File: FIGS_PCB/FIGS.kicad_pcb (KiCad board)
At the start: 2 copper layers, 54.1 x 52.8 mm, 66 parts, among them IC1 CY8C4245AXI-483, J1 CAPSENSE_CON, J10 HAPTIC_M, J2 FINGCONN, J3 BLUTH, J4 IMU, J5 SERVO_0, J6 SERVO_1, J7 SERVO_2, J8 PROGRAMMER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

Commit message: PCB changed
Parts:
- removed R1, R3, R5, R7: 5.6k, Resistor_SMD:R_1206_3216Metric_Pad1.30x1.75mm_HandSolder
- removed R10, R9: 0, Resistor_SMD:R_1206_3216Metric_Pad1.30x1.75mm_HandSolder
- removed R2, R4, R6, R8: nc, Resistor_SMD:R_1206_3216Metric_Pad1.30x1.75mm_HandSolder
- added H1: MountingHole, MountingHole:MountingHole_2.7mm, F.Cu at (33.0, 38.0)
- added H2: MountingHole, MountingHole:MountingHole_2.7mm, F.Cu at (35.0, 76.0)
- added H3: MountingHole, MountingHole:MountingHole_2.7mm, F.Cu at (80.0, 39.5)
- added TP1: TestPoint, TestPoint:TestPoint_Pad_D3.0mm, F.Cu at (64.5, 54.9)
- added TP2: TestPoint, TestPoint:TestPoint_Pad_D3.0mm, F.Cu at (40.6, 73.9)
- C11, C4: footprint Capacitor_Tantalum_SMD:CP_EIA-7260-28_AVX-M_Pad2.68x6.30mm_HandSolder -> Capacitor_Tantalum_SMD:CP_EIA-7132-20_AVX-U_Pad2.72x3.50mm_HandSolder
- C2, C3, C5, C6, R11, R14, R18, R20, R24, R26: moved to B.Cu
- J1: footprint Connector_PinHeader_1.27mm:PinHeader_1x08_P1.27mm_Horizontal -> Connector_PinHeader_2.54mm:PinHeader_1x08_P2.54mm_Horizontal
- J10: footprint Connector_PinHeader_1.27mm:PinHeader_1x02_P1.27mm_Horizontal -> Connector_PinHeader_2.54mm:PinHeader_1x02_P2.54mm_Horizontal; moved to F.Cu
- J2: footprint Connector_PinHeader_1.27mm:PinHeader_2x04_P1.27mm_Vertical -> Connector_PinHeader_2.54mm:PinHeader_2x04_P2.54mm_Horizontal
- J3: footprint Connector_PinHeader_1.27mm:PinHeader_1x04_P1.27mm_Horizontal -> Connector_PinHeader_2.54mm:PinHeader_1x04_P2.54mm_Horizontal
- J4: footprint Connector_PinHeader_1.27mm:PinHeader_1x04_P1.27mm_Horizontal -> Connector_PinHeader_2.54mm:PinHeader_1x04_P2.54mm_Horizontal; moved to F.Cu
- J5, J6, J7, J9: footprint Connector_PinHeader_1.27mm:PinHeader_1x03_P1.27mm_Horizontal -> Connector_PinHeader_2.54mm:PinHeader_1x03_P2.54mm_Horizontal
- J8: footprint Connector_PinHeader_1.27mm:PinHeader_2x05_P1.27mm_Horizontal -> Connector_PinHeader_2.54mm:PinHeader_2x05_P2.54mm_Vertical; moved to F.Cu
- R15: moved to F.Cu
- moved BT1 57.7 mm to (32.5, 87.1)
- moved C4 54.9 mm to (43.7, 84.8)
- moved SW1 53.2 mm to (36.8, 87.1), turned to 90 degrees
- moved C7 42.6 mm to (47.2, 83.1), turned to 90 degrees
- moved U1 38.3 mm to (52.1, 82.1), turned to 90 degrees
- moved D7 37.8 mm to (38.4, 68.3), turned to 90 degrees
- moved R15 37.1 mm to (62.2, 77.5)
- moved J10 36.1 mm to (41.1, 69.6), turned to 180 degrees
- moved J2 33.0 mm to (32.0, 32.5), turned to 90 degrees
- moved D2 32.9 mm to (36.3, 42.7)
- moved D4 30.7 mm to (41.1, 40.1), turned to 270 degrees
- moved D1 30.6 mm to (36.3, 48.0)
- moved Q5 30.0 mm to (45.2, 66.8), turned to 90 degrees
- moved R28 29.7 mm to (45.7, 70.4), turned to 180 degrees
- moved D3 27.7 mm to (41.1, 45.5)
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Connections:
- IC1 pad 24: /Rx_1 -> /BT_UART_TX
- IC1 pad 25: /Tx_1 -> /BT_UART_RX
- J3 pad 1: +3V3 -> /BT_UART_RX
- J3 pad 3: /BT_UART_RX -> GNDA
- J3 pad 4: GNDA -> +3V3
- J4 pad 2: /IMU_SCL -> /IMU_SDA
- J4 pad 3: /IMU_SDA -> /IMU_SCL
- J5 pad 1: +BATT -> /CTRLS0
- J5 pad 2: /CTRLS0 -> +BATT
- J6 pad 1: +BATT -> /CTRLS1
- J6 pad 2: /CTRLS1 -> +BATT
- J7 pad 1: +BATT -> /CTRLS2
- J7 pad 2: /CTRLS2 -> +BATT
- J8 pad 1: +3V3 -> GNDA
- J8 pad 10: /KP_TX -> /TUNER_SDA
- J8 pad 2: GNDA -> +3V3
- J8 pad 3: /SWD_IO -> /XRES
- J8 pad 4: /XRES -> /SWD_IO
- J8 pad 5: /SWD_CLK -> Net-(J8-Pad5)
- J8 pad 6: Net-(J8-Pad6) -> /SWD_CLK
- J8 pad 7: /TUNER_SCL -> /KP_TX
- J8 pad 8: /KP_RX -> /TUNER_SCL
- J8 pad 9: /TUNER_SDA -> /KP_RX
- J9 pad 1: +BATT -> /CTRLS3
- J9 pad 2: /CTRLS3 -> +BATT
- R11 pad 2: /IMU_SDA -> /IMU_SCL
- R12 pad 1: /Rx_1 -> /BT_UART_RX
- R12 pad 2: /KP_TX -> /KP_RX
- R13 pad 1: /KP_RX -> /KP_TX
- R13 pad 2: /Tx_1 -> /BT_UART_TX
- R14 pad 2: /IMU_SCL -> /IMU_SDA
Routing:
- net +BATT: track 35.3 -> 148.3 mm
- net +3V3: track 75.2 -> 151.4 mm, vias 2 -> 1
- net /Tx_1: track 33.8 -> 0.00 mm
- net /Rx_1: track 28.9 -> 0.00 mm
- net /BT_UART_RX: track 7.16 -> 30.4 mm
- net /BT_UART_TX: track 9.24 -> 30.7 mm
- net /SERVOS_OUT0: track 29.6 -> 17.1 mm
- net /SERVOS_OUT2: track 19.5 -> 31.7 mm
- net /SWD_IO: track 11.2 -> 22.4 mm
- net /TUNER_SDA: track 19.5 -> 8.45 mm
- net /SERVOS_LED1: track 21.8 -> 12.2 mm
- net /STATUS_LED1: track 3.49 -> 12.4 mm
- net /SWD_CLK: track 12.0 -> 20.6 mm
- net /SERVOS_OUT3: track 14.4 -> 22.8 mm
- net /TUNER_SCL: track 19.1 -> 11.3 mm
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- removed copper zone on B.Cu, net +3V3
- removed copper zone on B.Cu, net +BATT
- removed copper zone on B.Cu, net GNDA
- removed copper zone on F.Cu, net GNDA
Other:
- board size 54.1 x 52.8 mm -> 55 x 70 mm
- net class Default: clearance 0.25 -> 0.254; trace_width 0.4 -> 0.4064; via_dia 1.75 -> 1.9558; via_drill 0.55 -> 0.5588
- net class ThickPower: clearance 0.5 -> 0.254; trace_width 0.75 -> 1.016; via_dia 1.75 -> 1.9558; via_drill 0.55 -> 0.5588
- rule trace_clearance: 0.25 -> 0.254

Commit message: Finished PCB with LOGO and text
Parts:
- added G***: LOGO, FIGSGRAPHIC:GraphicFIGS10x10, F.Cu at (51.5, 83.0)
- moved R15 0.53 mm to (62.2, 78.0)
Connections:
- U1 pad 4: (no net) -> +3V3
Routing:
- net +3V3: track 151.4 -> 154.2 mm
- added copper zone on B.Cu, net GNDA
- added copper zone on F.Cu, net GNDA
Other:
- board text added: "FIGS"

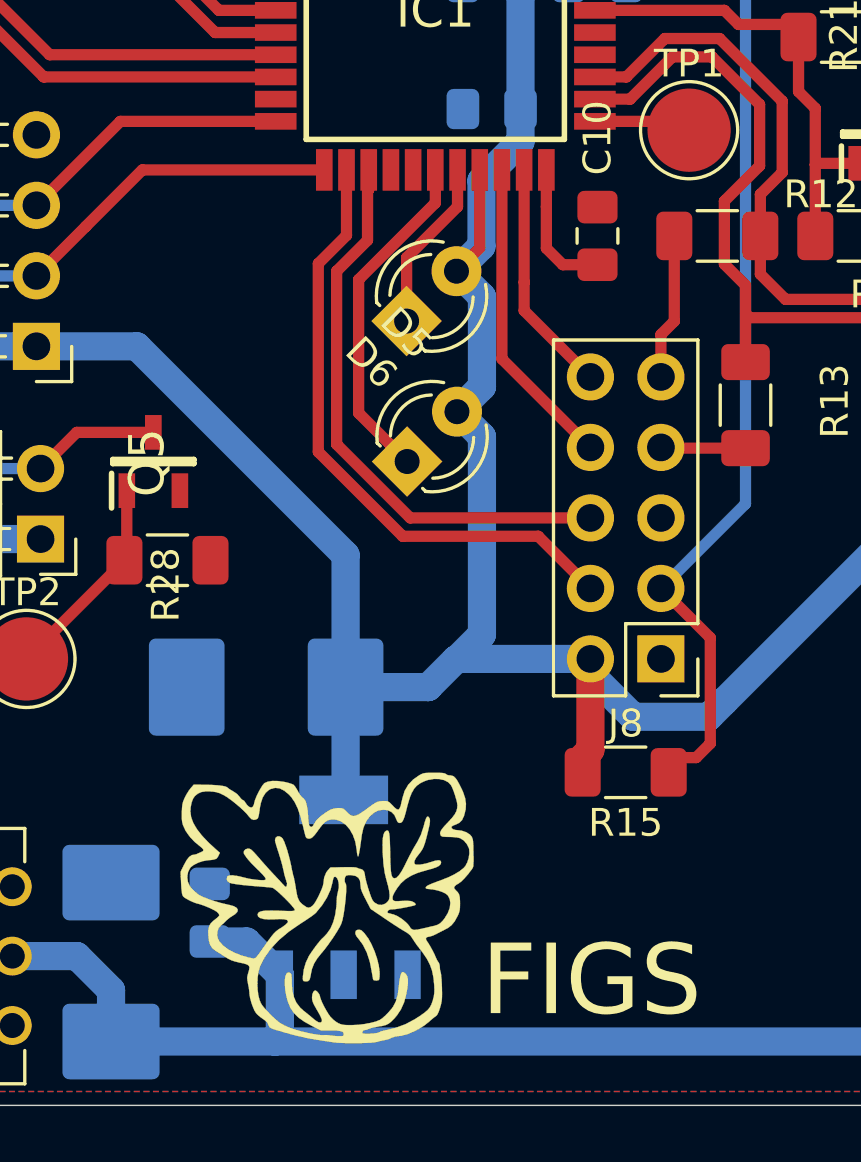
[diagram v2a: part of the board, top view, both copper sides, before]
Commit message: added Pullups on tuner SCL/SDA lines
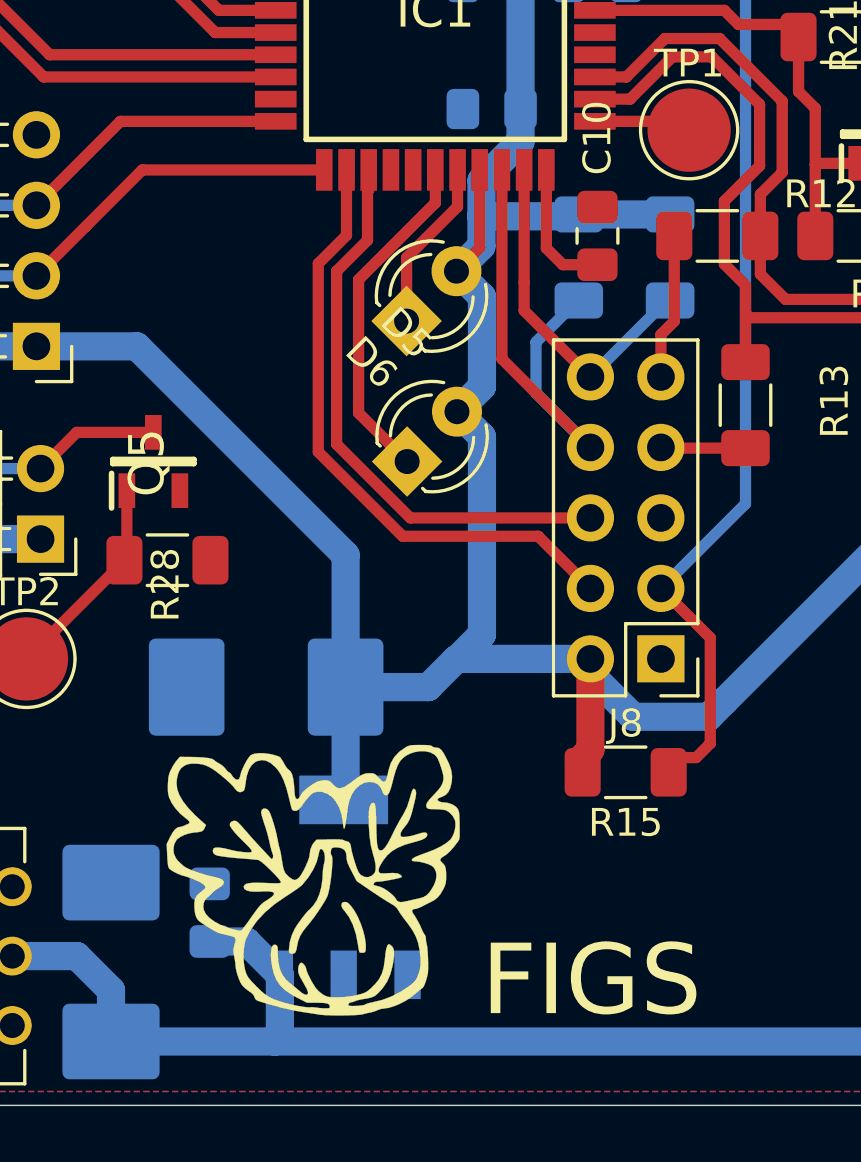
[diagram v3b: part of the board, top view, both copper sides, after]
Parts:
- added R1: 10k, Resistor_SMD:R_1206_3216Metric_Pad1.30x1.75mm_HandSolder, B.Cu at (63.8, 59.5)
- added R2: 10k, Resistor_SMD:R_1206_3216Metric_Pad1.30x1.75mm_HandSolder, B.Cu at (60.5, 59.5)
- moved G*** 1.12 mm to (51.0, 82.0)
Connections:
- U1 pad 4: +3V3 -> (no net)
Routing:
- net +3V3: track 154.2 -> 161.0 mm
- net /TUNER_SCL: track 11.3 -> 18.1 mm
- net /TUNER_SDA: track 8.45 -> 12.5 mm
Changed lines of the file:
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@@
     (thickness 1.6)
     (drawings 10)
-    (tracks 339)
+    (tracks 349)
     (zones 0)
-    (modules 62)
+    (modules 64)
     (nets 51)
   )
@@
   )
   (module FIGSGRAPHIC:GraphicFIGS10x10 (layer F.Cu)
-    (at 51.5 83)
+    (at 51 82)
     (fp_text reference G*** (at 0 0) (layer F.SilkS) hide
       (effects (font (size 1.524 1.524) (thickness 0.3)))
@@
       (xy 1.099118 0.672988) (xy 1.161492 0.674975)) (layer F.SilkS) (width 0.01))
   )
+  (module Resistor_SMD:R_1206_3216Metric_Pad1.30x1.75mm_HandSolder (layer B.Cu)
+    (at 60.54 59.45 270)
+    (descr "Resistor SMD 1206 (3216 Metric), square (rectangular) end terminal, IPC_7351 nominal with elongated pad for handsoldering. (Body size source: IPC-SM-782 page 72, https://www.pcb-3d.com/wordpress/wp-content/uploads/ipc-sm-782a_amendment_1_and_2.pdf), generated with kicad-footprint-generator")
+    (tags "resistor handsolder")
+    (attr smd)
+    (fp_text reference R2 (at 0 1.82 90) (layer B.SilkS)
+      (effects (font (size 1 1) (thickness 0.15)) (justify mirror))
+    )
+    (fp_text value 10k (at 0 -1.82 90) (layer B.Fab)
+      (effects (font (size 1 1) (thickness 0.15)) (justify mirror))
+    )
+    (fp_line (start 2.45 -1.12) (end -2.45 -1.12) (layer B.CrtYd) (width 0.05))
+    (fp_line (start 2.45 1.12) (end 2.45 -1.12) (layer B.CrtYd) (width 0.05))
+    (fp_line (start -2.45 1.12) (end 2.45 1.12) (layer B.CrtYd) (width 0.05))
+    (fp_line (start -2.45 -1.12) (end -2.45 1.12) (layer B.CrtYd) (width 0.05))
+    (fp_line (start -0.727064 -0.91) (end 0.727064 -0.91) (layer B.SilkS) (width 0.12))
+    (fp_line (start -0.727064 0.91) (end 0.727064 0.91) (layer B.SilkS) (width 0.12))
+    (fp_line (start 1.6 -0.8) (end -1.6 -0.8) (layer B.Fab) (width 0.1))
+    (fp_line (start 1.6 0.8) (end 1.6 -0.8) (layer B.Fab) (width 0.1))
+    (fp_line (start -1.6 0.8) (end 1.6 0.8) (layer B.Fab) (width 0.1))
+    (fp_line (start -1.6 -0.8) (end -1.6 0.8) (layer B.Fab) (width 0.1))
+    (fp_text user %R (at 0 0 90) (layer B.Fab)
+      (effects (font (size 0.8 0.8) (thickness 0.12)) (justify mirror))
+    )
+    (pad 2 smd roundrect (at 1.55 0 270) (size 1.3 1.75) (layers B.Cu B.Paste B.Mask) (roundrect_rratio 0.192308)
+      (net 31 /TUNER_SCL))
+    (pad 1 smd roundrect (at -1.55 0 270) (size 1.3 1.75) (layers B.Cu B.Paste B.Mask) (roundrect_rratio 0.192308)
+      (net 3 +3V3))
+    (model ${KISYS3DMOD}/Resistor_SMD.3dshapes/R_1206_3216Metric.wrl
+      (at (xyz 0 0 0))
+      (scale (xyz 1 1 1))
+      (rotate (xyz 0 0 0))
+    )
+  )
+  (module Resistor_SMD:R_1206_3216Metric_Pad1.30x1.75mm_HandSolder (layer B.Cu)
+    (at 63.83 59.45 270)
+    (descr "Resistor SMD 1206 (3216 Metric), square (rectangular) end terminal, IPC_7351 nominal with elongated pad for handsoldering. (Body size source: IPC-SM-782 page 72, https://www.pcb-3d.com/wordpress/wp-content/uploads/ipc-sm-782a_amendment_1_and_2.pdf), generated with kicad-footprint-generator")
+    (tags "resistor handsolder")
+    (attr smd)
+    (fp_text reference R1 (at 0 1.82 90) (layer B.SilkS)
+      (effects (font (size 1 1) (thickness 0.15)) (justify mirror))
+    )
+    (fp_text value 10k (at 0 -1.82 90) (layer B.Fab)
+      (effects (font (size 1 1) (thickness 0.15)) (justify mirror))
+    )
+    (fp_line (start 2.45 -1.12) (end -2.45 -1.12) (layer B.CrtYd) (width 0.05))
+    (fp_line (start 2.45 1.12) (end 2.45 -1.12) (layer B.CrtYd) (width 0.05))
+    (fp_line (start -2.45 1.12) (end 2.45 1.12) (layer B.CrtYd) (width 0.05))
+    (fp_line (start -2.45 -1.12) (end -2.45 1.12) (layer B.CrtYd) (width 0.05))
+    (fp_line (start -0.727064 -0.91) (end 0.727064 -0.91) (layer B.SilkS) (width 0.12))
+    (fp_line (start -0.727064 0.91) (end 0.727064 0.91) (layer B.SilkS) (width 0.12))
+    (fp_line (start 1.6 -0.8) (end -1.6 -0.8) (layer B.Fab) (width 0.1))
+    (fp_line (start 1.6 0.8) (end 1.6 -0.8) (layer B.Fab) (width 0.1))
+    (fp_line (start -1.6 0.8) (end 1.6 0.8) (layer B.Fab) (width 0.1))
+    (fp_line (start -1.6 -0.8) (end -1.6 0.8) (layer B.Fab) (width 0.1))
+    (fp_text user %R (at 0 0 90) (layer B.Fab)
+      (effects (font (size 0.8 0.8) (thickness 0.12)) (justify mirror))
+    )
+    (pad 2 smd roundrect (at 1.55 0 270) (size 1.3 1.75) (layers B.Cu B.Paste B.Mask) (roundrect_rratio 0.192308)
+      (net 30 /TUNER_SDA))
+    (pad 1 smd roundrect (at -1.55 0 270) (size 1.3 1.75) (layers B.Cu B.Paste B.Mask) (roundrect_rratio 0.192308)
+      (net 3 +3V3))
+    (model ${KISYS3DMOD}/Resistor_SMD.3dshapes/R_1206_3216Metric.wrl
+      (at (xyz 0 0 0))
+      (scale (xyz 1 1 1))
+      (rotate (xyz 0 0 0))
+    )
+  )
   (module TestPoint:TestPoint_Pad_D3.0mm (layer F.Cu)
     (at 40.64 73.914)
@@
     (fp_line (start 4.275 3.6) (end 4.275 -3.6) (layer Dwgs.User) (width 0.05))
     (fp_line (start -4.275 3.6) (end 4.275 3.6) (layer Dwgs.User) (width 0.05))
-    (pad 4 smd rect (at 3.15 0 90) (size 1.75 3.200001) (layers B.Cu B.Paste B.Mask)
-      (net 3 +3V3))
+    (pad 4 smd rect (at 3.15 0 90) (size 1.75 3.200001) (layers B.Cu B.Paste B.Mask))
     (pad 3 smd rect (at -3.15 -2.3) (size 0.95 1.75) (layers B.Cu B.Paste B.Mask)
       (net 4 +BATT))
@@
   (segment (start 58.4415 49.53) (end 60.1765 49.53) (width 1.016) (layer B.Cu) (net 3))
   (segment (start 58.4415 54.102) (end 58.4415 49.53) (width 1.016) (layer B.Cu) (net 3))
-  (segment (start 57.033999 59.044001) (end 57.033999 56.68143) (width 1.016) (layer B.Cu) (net 3))
   (segment (start 56.134 59.944) (end 57.033999 59.044001) (width 1.016) (layer B.Cu) (net 3))
   (segment (start 58.4415 55.273929) (end 58.4415 54.102) (width 1.016) (layer B.Cu) (net 3))
@@
   (segment (start 38.230398 45.212) (end 40.770398 42.672) (width 1.016) (layer B.Cu) (net 3))
   (segment (start 36.322 45.212) (end 38.230398 45.212) (width 1.016) (layer B.Cu) (net 3))
+  (segment (start 60.473999 57.966001) (end 60.54 57.9) (width 1.016) (layer B.Cu) (net 3))
+  (segment (start 57.033999 57.966001) (end 60.473999 57.966001) (width 1.016) (layer B.Cu) (net 3))
+  (segment (start 57.033999 59.044001) (end 57.033999 57.966001) (width 1.016) (layer B.Cu) (net 3))
+  (segment (start 57.033999 57.966001) (end 57.033999 56.68143) (width 1.016) (layer B.Cu) (net 3))
+  (segment (start 60.54 57.9) (end 63.83 57.9) (width 1.016) (layer B.Cu) (net 3))
   (segment (start 71.54 26.01) (end 71.55 26) (width 1.016) (layer B.Cu) (net 4))
   (segment (start 71.54 30) (end 71.54 26.01) (width 1.016) (layer B.Cu) (net 4))
@@
   (segment (start 58.572 61.366) (end 58.572 60.35) (width 0.4064) (layer F.Cu) (net 30))
   (segment (start 60.96 63.754) (end 58.572 61.366) (width 0.4064) (layer F.Cu) (net 30))
+  (segment (start 63.714 61) (end 60.96 63.754) (width 0.4064) (layer B.Cu) (net 30))
+  (segment (start 63.83 61) (end 63.714 61) (width 0.4064) (layer B.Cu) (net 30))
   (segment (start 57.772 63.106) (end 60.96 66.294) (width 0.4064) (layer F.Cu) (net 31))
   (segment (start 57.772 56.296) (end 57.772 63.106) (width 0.4064) (layer F.Cu) (net 31))
+  (segment (start 60.54 61) (end 60.5 61) (width 0.4064) (layer B.Cu) (net 31))
+  (segment (start 60.5 61) (end 59 62.5) (width 0.4064) (layer B.Cu) (net 31))
+  (segment (start 59 64.334) (end 60.96 66.294) (width 0.4064) (layer B.Cu) (net 31))
+  (segment (start 59 62.5) (end 59 64.334) (width 0.4064) (layer B.Cu) (net 31))
   (segment (start 52.929201 57.052799) (end 52.929201 58.830799) (width 0.4064) (layer F.Cu) (net 34))
   (segment (start 52.972 56.296) (end 52.972 57.01) (width 0.4064) (layer F.Cu) (net 34))
